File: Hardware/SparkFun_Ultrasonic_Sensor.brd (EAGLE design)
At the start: 45 x 21.5 mm, 76 parts, among them J4 Vertical Qwiic Connector, J6 Vertical Qwiic Connector, Q1 600mA/40V, U5 ULTRASONIC_SENSOR_TRANSMITTER, U6 LMV324, U7 STM8L051F3, U8 SP3232EB, U9 ULTRASONIC_SENSOR_RECEIVER

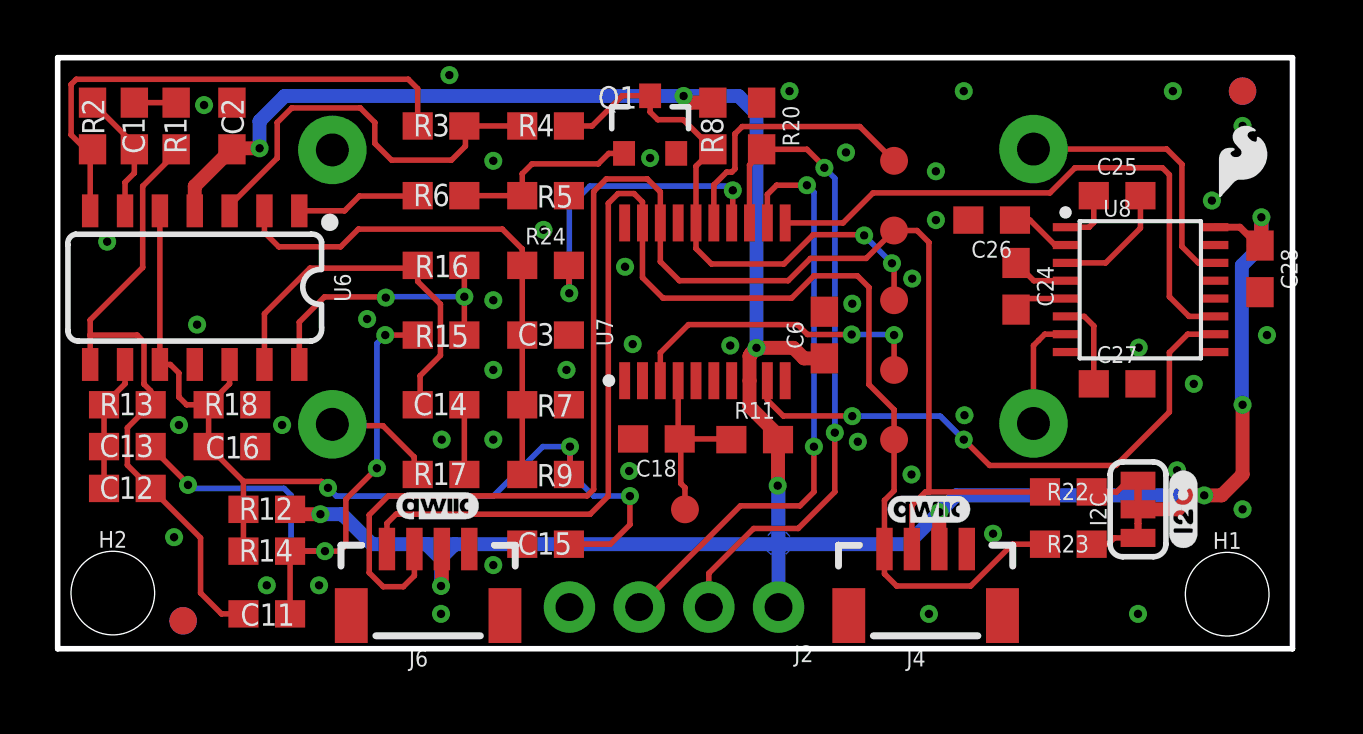
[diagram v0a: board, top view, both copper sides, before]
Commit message: Changes the size and placement of parts so that they sit at reasonable dimensions
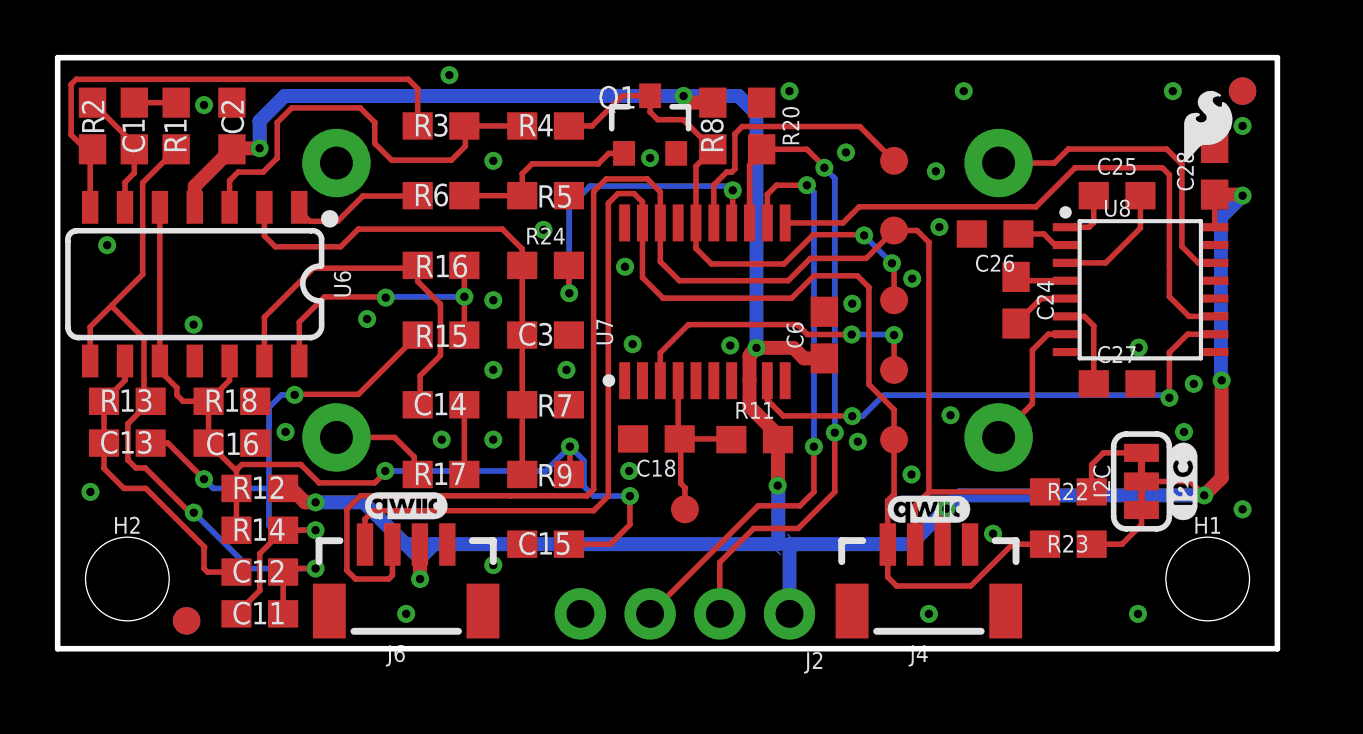
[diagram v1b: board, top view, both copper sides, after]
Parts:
- moved C12 5.71 mm to (7.37, 2.79)
- moved C28 3.92 mm to (42.2, 17.4), turned to 90 degrees
- moved U$12 2.93 mm to (22.0, 14.2)
- moved U$10 2.33 mm to (22.0, 16.1)
- moved U$6 1.80 mm to (41.9, 19.1)
- moved U$11 1.45 mm to (22.0, 17.7)
- moved U$8 1.42 mm to (34.3, 3.17)
- moved U5 1.37 mm to (34.3, 12.7)
- moved LOGO3 1.14 mm to (12.7, 5.21)
- moved I2C 1.02 mm to (39.5, 6.10)
- moved U$7 1.02 mm to (41.0, 6.10)
- moved LOGO2 0.92 mm to (22.0, 19.3)
- moved H1 0.90 mm to (41.9, 2.54)
- moved J6 0.82 mm to (12.7, 4.57)
- moved R12 0.80 mm to (7.37, 5.84)
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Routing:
- net N$9: track 4.83 -> 11.1 mm
- net N$10: track 23.8 -> 26.8 mm, vias 0 -> 2
- net DIN2: track 21.2 -> 19.5 mm
- net N$48: track 10.1 -> 11.6 mm
- net N$19: track 1.86 -> 2.99 mm
- net 3.3V: track 103.5 -> 102.4 mm
- net N$49: track 4.21 -> 5.17 mm
- net N$20: track 1.78 -> 2.64 mm
- net N$31: track 37.1 -> 36.4 mm
- net SCL: track 51.1 -> 51.7 mm
- net SDA: track 56.6 -> 57.2 mm
- net N$12: track 22.7 -> 22.5 mm, vias 4 -> 3
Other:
- board size 45 x 21.5 mm -> 44.5 x 21.5 mm

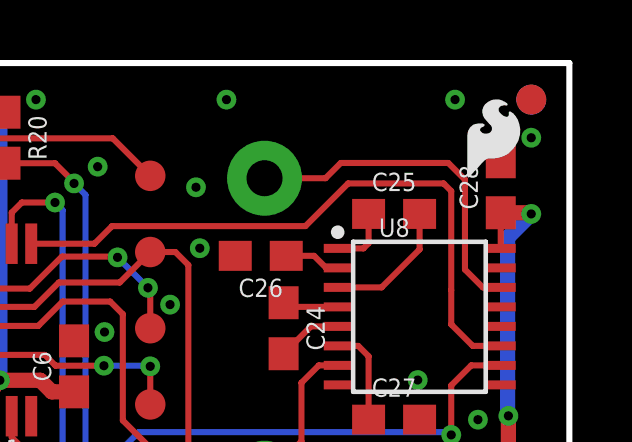
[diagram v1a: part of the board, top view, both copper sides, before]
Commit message: Moves SparkFun logo
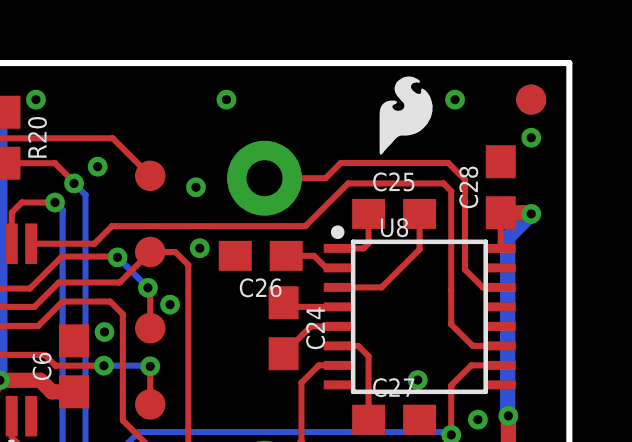
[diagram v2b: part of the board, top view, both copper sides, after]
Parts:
- moved U$6 3.02 mm to (39.0, 19.8)
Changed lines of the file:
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@@
 <element name="LOGO4" library="SparkFun-Aesthetics" package="OSHW-LOGO-S" value="OSHW-LOGOS" x="2.159" y="19.304" smashed="yes" rot="MR0"/>
 <element name="U$5" library="SparkFun-Aesthetics" package="QWIIC_3MM" value="" x="31.75" y="5.08" smashed="yes"/>
-<element name="U$6" library="SparkFun-Aesthetics" package="SFE_LOGO_FLAME_.1" value="" x="41.91" y="19.05" smashed="yes"/>
+<element name="U$6" library="SparkFun-Aesthetics" package="SFE_LOGO_FLAME_.1" value="" x="38.989" y="19.812" smashed="yes"/>
 <element name="U$7" library="bot" package="#I2C#16" value="" x="41.021" y="6.096" smashed="yes" rot="R90"/>
 </elements>

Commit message: Adds a few more measures
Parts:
- moved FRAME1 80.3 mm to (72.8, -7.60)
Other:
- board text added: "Units In Inches"
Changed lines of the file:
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@@
 HASL Lead Free
 Material: TG135-140</text>
-<text x="24.13" y="-13.97" size="1.778" layer="51" font="vector">NOA Labs</text>
-<text x="4.318" y="-16.51" size="1.778" layer="51" font="vector">Revised By: Elias Santistevan</text>
+<text x="102.87" y="-7.62" size="1.778" layer="51" font="vector">NOA Labs</text>
+<text x="84.328" y="-10.16" size="1.778" layer="51" font="vector">Revised By: Elias Santistevan</text>
 <dimension x1="0" y1="21.5392" x2="44.45" y2="21.5392" x3="22.225" y3="31.75" textsize="1.778" layer="47" unit="inch"/>
 <dimension x1="10.16" y1="12.7" x2="0" y2="12.7" x3="5.08" y3="24.13" textsize="1.778" layer="47" unit="inch"/>
 <dimension x1="12.7" y1="4.572" x2="0" y2="4.572" x3="6.35" y3="-3.81" textsize="1.778" layer="47" unit="inch"/>
-<dimension x1="31.75" y1="4.572" x2="44.45" y2="4.572" x3="38.1" y3="-3.81" textsize="1.778" layer="47" unit="inch"/>
+<dimension x1="31.75" y1="4.572" x2="44.45" y2="4.572" x3="38.1" y3="-6.35" textsize="1.778" layer="47" unit="inch"/>
 <dimension x1="34.29" y1="12.7" x2="44.45" y2="12.7" x3="39.37" y3="24.13" textsize="1.778" layer="47" unit="inch"/>
 <dimension x1="10.16" y1="12.7" x2="34.29" y2="12.7" x3="22.225" y3="24.13" textsize="1.778" layer="47" unit="inch"/>
+<dimension x1="2.54" y1="2.54" x2="2.54" y2="0" x3="-2.54" y3="1.27" textsize="1.778" layer="47" unit="inch"/>
+<dimension x1="41.91" y1="2.54" x2="44.45" y2="2.54" x3="43.18" y3="-2.54" textsize="1.778" layer="47" unit="inch"/>
+<dimension x1="26.67" y1="1.27" x2="0" y2="1.27" x3="13.335" y3="-10.16" textsize="1.778" layer="47" unit="inch"/>
+<text x="12.7" y="-19.05" size="1.778" layer="47" font="vector">Units In Inches</text>
 </plain>
 <attributes>
@@
 <attribute name="VALUE" x="38.0746" y="9.8298" size="0.6096" layer="27" font="vector" ratio="20"/>
 </element>
-<element name="FRAME1" library="SparkFun-Aesthetics" package="CREATIVE_COMMONS" value="FRAME-LEDGER" x="-7.16" y="-13.95" smashed="yes">
-<attribute name="DESIGNER" value="NOA Labs" x="-7.16" y="-13.95" size="1.778" layer="27" display="off"/>
-<attribute name="REV" value="v11" x="-7.16" y="-13.95" size="1.778" layer="27" display="off"/>
+<element name="FRAME1" library="SparkFun-Aesthetics" package="CREATIVE_COMMONS" value="FRAME-LEDGER" x="72.85" y="-7.6" smashed="yes">
+<attribute name="DESIGNER" value="NOA Labs" x="72.85" y="-7.6" size="1.778" layer="27" display="off"/>
+<attribute name="REV" value="v11" x="72.85" y="-7.6" size="1.778" layer="27" display="off"/>
 </element>
 <element name="C24" library="SparkFun-Capacitors" package="0603" value="0.1uF" x="34.925" y="12.7" smashed="yes" rot="R270">
